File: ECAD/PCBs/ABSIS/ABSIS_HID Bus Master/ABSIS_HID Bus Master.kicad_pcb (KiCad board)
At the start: 2 copper layers, 90.8 x 53.3 mm, 19 parts, among them J1 Molex_Mini-Fit_Jr._2x04, J2 Mini-Fit Jr. 2x03, U0 ProMicro_5V/16Hz, U1 MAX487EESA+T

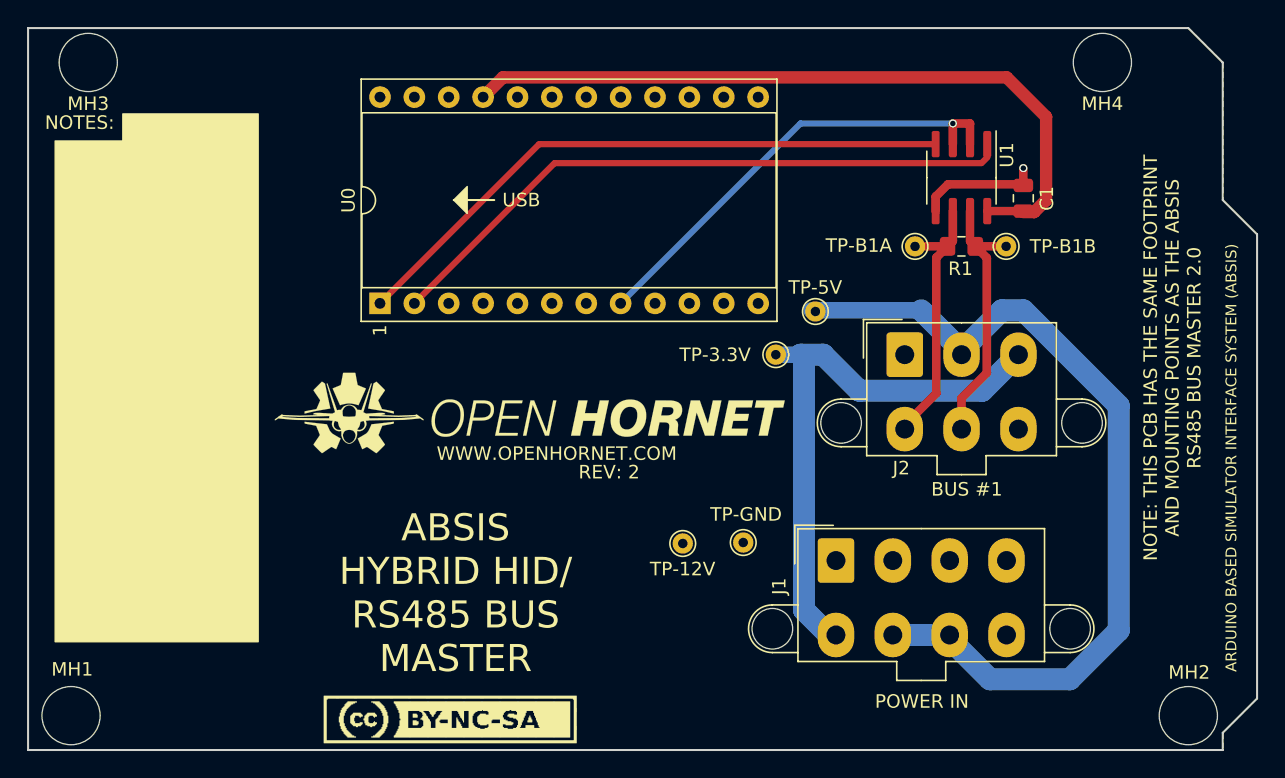
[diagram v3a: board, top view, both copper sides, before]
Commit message: Updated ABSIS_HID Bus Master
Added 1N5819WS (D1) between 12V Supply and RAW pin of Pro-Micro
Updated to Rev 3.
Closes #995
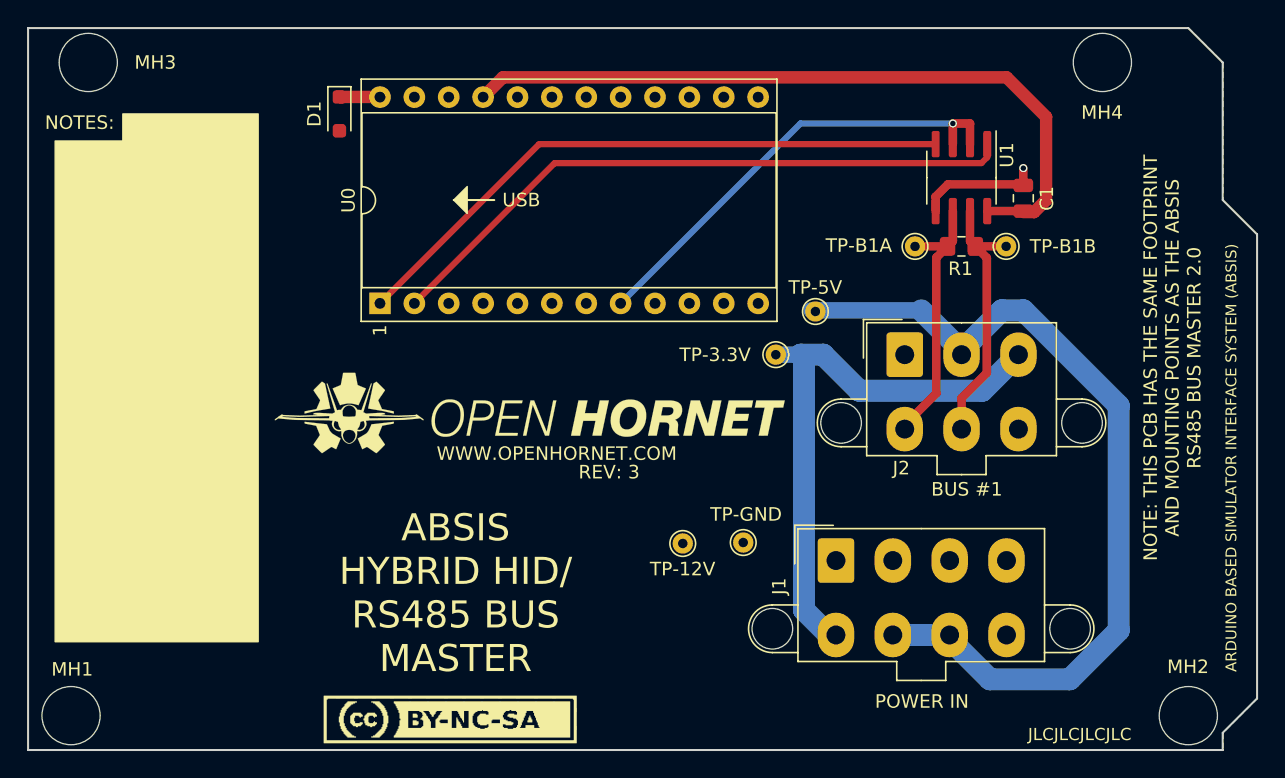
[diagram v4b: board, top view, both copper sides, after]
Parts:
- added D1: 1N5819WS, Diode_SMD:D_SOD-323_HandSoldering, F.Cu at (137.2, 74.7)
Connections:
- U0 pad 24: /+12V_SUPPLY -> Net-(D1-K)
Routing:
- net Net-(D1-K): track 0.00 -> 3.00 mm
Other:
- board text added: "JLCJLCJLCJLC"
- board text added: "REV: 3"
- board text removed: "REV: 2"
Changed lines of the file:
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@@
   (title_block
     (title "ABSIS HID Bus Master")
-    (date "2023-02-10")
-    (rev "2")
+    (date "2023-11-05")
+    (rev "3")
     (company "www.openhornet.com")
     (comment 1 "License:  CC BY-NC-SA")
@@
   (net 25 "unconnected-(U0-A3-Pad20)")
   (net 26 "/TX0_D1")
+  (net 27 "Net-(D1-K)")
   (footprint "OH_Footprints:MountingHole_6-32_PHS" (layer "F.Cu")
     (at 117.348 119.126)
@@
     (property "ki_description" "6-32 PHS Hole with back fill keepout area, 4.3mm")
     (attr through_hole board_only exclude_from_pos_files exclude_from_bom)
-    (fp_text reference "MH2" (at 0.065 -3.19) (layer "F.SilkS")
+    (fp_text reference "MH2" (at -0.025 -3.61) (layer "F.SilkS")
         (effects (font (size 1 1) (thickness 0.15)))
     )
@@
     (property "ki_description" "6-32 PHS Hole with back fill keepout area, 4.3mm")
     (attr through_hole board_only exclude_from_pos_files exclude_from_bom)
-    (fp_text reference "MH3" (at 0 3.048) (layer "F.SilkS")
+    (fp_text reference "MH3" (at 4.955 0) (layer "F.SilkS")
         (effects (font (size 1 1) (thickness 0.15)))
     )
@@
     (property "ki_description" "6-32 PHS Hole with back fill keepout area, 4.3mm")
     (attr through_hole board_only exclude_from_pos_files exclude_from_bom)
-    (fp_text reference "MH4" (at 0 3.048) (layer "F.SilkS")
+    (fp_text reference "MH4" (at -0.025 3.7) (layer "F.SilkS")
         (effects (font (size 1 1) (thickness 0.15)))
     )
@@
     (property "Sheetname" "")
     (property "Silkscreen" "POWER IN")
-    (attr through_hole)
+    (attr through_hole exclude_from_pos_files)
     (fp_text reference "J1" (at -4.191 1.905 90) (layer "F.SilkS")
         (effects (font (size 1 1) (thickness 0.15)))
@@
     (property "ki_description" "Generic connector, double row, 02x03, top/bottom pin numbering scheme (row 1: 1...pins_per_row, row2: pins_per_row+1 ... num_pins), script generated (kicad-library-utils/schlib/autogen/connector/)")
     (property "ki_keywords" "connector")
-    (attr through_hole)
+    (attr through_hole exclude_from_pos_files)
     (fp_text reference "J2" (at -0.254 8.382) (layer "F.SilkS")
         (effects (font (size 1 1) (thickness 0.15)))
@@
     (property "Sheetname" "")
     (property "ki_description" "CC License, BY-NC-SA, no symbols, Small")
-    (attr board_only exclude_from_bom)
+    (attr board_only exclude_from_pos_files exclude_from_bom)
     (fp_text reference "LOGO3" (at 0 5) (layer "F.SilkS") hide
         (effects (font (size 1.524 1.524) (thickness 0.3)))
@@
     (property "Sheetfile" "ABSIS_HID Bus Master.kicad_sch")
     (property "Sheetname" "")
-    (attr through_hole)
+    (attr through_hole exclude_from_pos_files)
     (fp_text reference "U0" (at 7.62 -2.33 90) (layer "F.SilkS")
         (effects (font (size 1 1) (thickness 0.15)))
@@
       (net 1 "GND") (pinfunction "GND") (pintype "power_in"))
     (pad "24" thru_hole oval (at 15.24 0 90) (size 1.6 1.6) (drill 0.8) (layers "*.Cu" "*.Mask")
-      (net 3 "/+12V_SUPPLY") (pinfunction "RAW") (pintype "power_in"))
+      (net 27 "Net-(D1-K)") (pinfunction "RAW") (pintype "power_in"))
     (model "${KICAD_USER_OH_3DMODELS}/DIP-24_W15.24mm_Socket.step"
       (offset (xyz 0 0 0))
@@
       (net 4 "/+5V_SUPPLY") (pinfunction "1") (pintype "passive"))
   )
+  (footprint "Diode_SMD:D_SOD-323_HandSoldering" (layer "F.Cu")
+    (at 137.173 74.666 -90)
+    (descr "SOD-323")
+    (tags "SOD-323")
+    (property "LCSC" "C191023")
+    (property "Manufacturer PN" "1N5819WS")
+    (property "Sheetfile" "ABSIS_HID Bus Master.kicad_sch")
+    (property "Sheetname" "")
+    (property "ki_description" "Schottky diode")
+    (property "ki_keywords" "diode Schottky")
+    (attr smd)
+    (fp_text reference "D1" (at 0 1.85 90) (layer "F.SilkS")
+        (effects (font (size 1 1) (thickness 0.15)))
+    )
+    (fp_text value "1N5819WS" (at 0.1 1.9 90) (layer "F.Fab")
+        (effects (font (size 1 1) (thickness 0.15)))
+    )
+    (fp_text user "${REFERENCE}" (at 0 -1.85 90) (layer "F.Fab")
+        (effects (font (size 1 1) (thickness 0.15)))
+    )
+    (fp_line (start -2.01 -0.85) (end -2.01 0.85)
+      (stroke (width 0.12) (type solid)) (layer "F.SilkS"))
+    (fp_line (start -2.01 -0.85) (end 1.25 -0.85)
+      (stroke (width 0.12) (type solid)) (layer "F.SilkS"))
+    (fp_line (start -2.01 0.85) (end 1.25 0.85)
+      (stroke (width 0.12) (type solid)) (layer "F.SilkS"))
+    (fp_line (start -2 -0.95) (end -2 0.95)
+      (stroke (width 0.05) (type solid)) (layer "F.CrtYd"))
+    (fp_line (start -2 -0.95) (end 2 -0.95)
+      (stroke (width 0.05) (type solid)) (layer "F.CrtYd"))
+    (fp_line (start -2 0.95) (end 2 0.95)
+      (stroke (width 0.05) (type solid)) (layer "F.CrtYd"))
+    (fp_line (start 2 -0.95) (end 2 0.95)
+      (stroke (width 0.05) (type solid)) (layer "F.CrtYd"))
+    (fp_line (start -0.9 -0.7) (end 0.9 -0.7)
+      (stroke (width 0.1) (type solid)) (layer "F.Fab"))
+    (fp_line (start -0.9 0.7) (end -0.9 -0.7)
+      (stroke (width 0.1) (type solid)) (layer "F.Fab"))
+    (fp_line (start -0.3 -0.35) (end -0.3 0.35)
+      (stroke (width 0.1) (type solid)) (layer "F.Fab"))
+    (fp_line (start -0.3 0) (end -0.5 0)
+      (stroke (width 0.1) (type solid)) (layer "F.Fab"))
+    (fp_line (start -0.3 0) (end 0.2 -0.35)
+      (stroke (width 0.1) (type solid)) (layer "F.Fab"))
+    (fp_line (start 0.2 -0.35) (end 0.2 0.35)
+      (stroke (width 0.1) (type solid)) (layer "F.Fab"))
+    (fp_line (start 0.2 0) (end 0.45 0)
+      (stroke (width 0.1) (type solid)) (layer "F.Fab"))
+    (fp_line (start 0.2 0.35) (end -0.3 0)
+      (stroke (width 0.1) (type solid)) (layer "F.Fab"))
+    (fp_line (start 0.9 -0.7) (end 0.9 0.7)
+      (stroke (width 0.1) (type solid)) (layer "F.Fab"))
+    (fp_line (start 0.9 0.7) (end -0.9 0.7)
+      (stroke (width 0.1) (type solid)) (layer "F.Fab"))
+    (pad "1" smd roundrect (at -1.25 0 270) (size 1 1) (layers "F.Cu" "F.Paste" "F.Mask") (roundrect_rratio 0.25)
+      (net 27 "Net-(D1-K)") (pinfunction "K") (pintype "passive"))
+    (pad "2" smd roundrect (at 1.25 0 270) (size 1 1) (layers "F.Cu" "F.Paste" "F.Mask") (roundrect_rratio 0.25)
+      (net 3 "/+12V_SUPPLY") (pinfunction "A") (pintype "passive"))
+    (model "${KICAD6_3DMODEL_DIR}/Diode_SMD.3dshapes/D_SOD-323.wrl"
+      (offset (xyz 0 0 0))
+      (scale (xyz 1 1 1))
+      (rotate (xyz 0 0 0))
+    )
+  )
   (footprint "OH_Footprints:TestPoint_THTPad_D1.5mm_Drill0.7mm" (layer "F.Cu")
     (at 169.418 92.456)
@@
     (effects (font (size 1 1) (thickness 0.15)))
   )
-  (gr_text "REV: 2" (at 157.103 101.136) (layer "F.SilkS")
+  (gr_text "REV: 3" (at 157.103 101.136) (layer "F.SilkS")
     (effects (font (size 1 1) (thickness 0.15)))
   )
@@
     (effects (font (size 0.8 0.8) (thickness 0.15)))
   )
+  (gr_text "JLCJLCJLCJLC" (at 191.873 120.516) (layer "F.SilkS")
+    (effects (font (size 0.9 0.9) (thickness 0.15)))
+  )
   (gr_text "NOTES:" (at 117.983 75.311) (layer "F.SilkS")
     (effects (font (size 1 1) (thickness 0.2)))
@@
   (segment (start 151.939 76.9) (end 140.173 88.666) (width 0.4572) (layer "F.Cu") (net 26))
   (segment (start 181.229 76.9) (end 151.939 76.9) (width 0.4572) (layer "F.Cu") (net 26))
+  (segment (start 137.173 73.416) (end 140.163 73.416) (width 0.9144) (layer "F.Cu") (net 27))
+  (segment (start 140.163 73.416) (end 140.173 73.426) (width 0.9144) (layer "F.Cu") (net 27))
   (zone (net 3) (net_name "/+12V_SUPPLY") (layer "F.Cu") (hatch edge 0.508)
     (connect_pads (clearance 0.508))

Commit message: Updated mounting holes
Updated PCB mounting holes to M3 clearance holes.
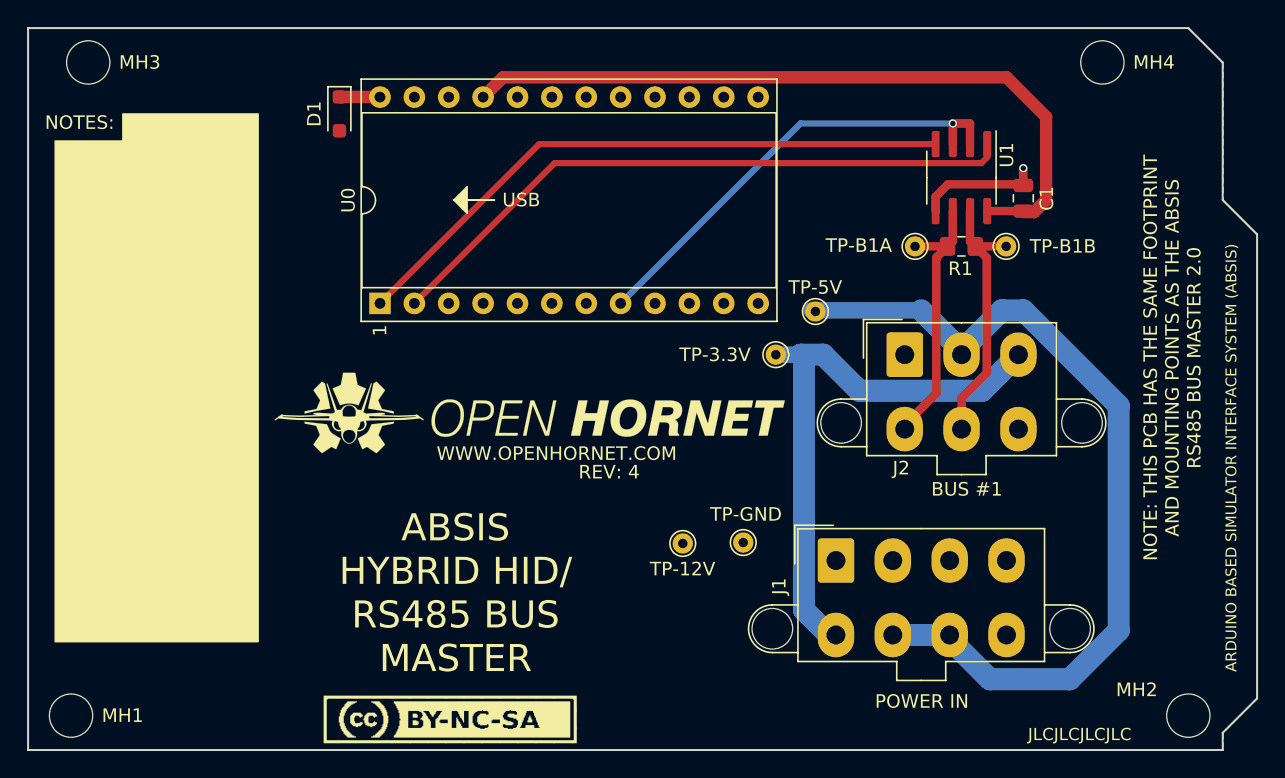
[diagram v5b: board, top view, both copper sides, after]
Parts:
- MH1, MH2, MH3, MH4: footprint OH_Footprints:MountingHole_6-32_PHS -> OH_Footprints:MountingHole_3.2mm_M3_DIN965
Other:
- board text added: "REV: 4"
- board text removed: "REV: 3"
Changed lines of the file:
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@@
   (title_block
     (title "ABSIS HID Bus Master")
-    (date "2023-11-05")
-    (rev "3")
+    (date "2023-12-10")
+    (rev "4")
     (company "www.openhornet.com")
     (comment 1 "License:  CC BY-NC-SA")
@@
   (net 26 "/TX0_D1")
   (net 27 "Net-(D1-K)")
-  (footprint "OH_Footprints:MountingHole_6-32_PHS" (layer "F.Cu")
+  (footprint "OH_Footprints:MountingHole_3.2mm_M3_DIN965" (layer "F.Cu")
     (at 117.348 119.126)
-    (descr "Mounting Hole for 6x32 PHS, 4.3mm")
+    (descr "Mounting Hole 3.2mm, no annular, M3, DIN965")
+    (tags "mounting hole 3.2mm no annular m3 din965")
     (property "Sheetfile" "ABSIS_HID Bus Master.kicad_sch")
     (property "Sheetname" "")
+    (property "Sim.Enable" "0")
     (property "exclude_from_bom" "")
-    (property "ki_description" "6-32 PHS Hole with back fill keepout area, 4.3mm")
-    (attr through_hole board_only exclude_from_pos_files exclude_from_bom)
-    (fp_text reference "MH1" (at 0.085 -3.42) (layer "F.SilkS")
+    (property "ki_description" "M3 hole with back fill keepout area, 3.2mm, DIN965")
+    (attr exclude_from_pos_files exclude_from_bom)
+    (fp_text reference "MH1" (at 3.81 0) (layer "F.SilkS")
         (effects (font (size 1 1) (thickness 0.15)))
     )
-    (fp_text value "6x32 / 4mm" (at -0.025 0) (layer "F.Fab") hide
+    (fp_text value "6x32 / 4mm" (at 0 8.636) (layer "F.Fab") hide
         (effects (font (size 1 1) (thickness 0.15)))
     )
-    (pad "" np_thru_hole circle (at 0 0) (size 4.3 4.3) (drill 4.3) (layers "F&B.Cu" "*.Mask")
-      (clearance 0.54))
+    (pad "" np_thru_hole circle (at 0 0) (size 3.2 3.2) (drill 3.2) (layers "F&B.Cu" "*.Mask")
+      (clearance 0.5))
   )
-  (footprint "OH_Footprints:MountingHole_6-32_PHS" (layer "F.Cu")
+  (footprint "OH_Footprints:MountingHole_3.2mm_M3_DIN965" (layer "F.Cu")
     (at 199.898 119.126)
-    (descr "Mounting Hole for 6x32 PHS, 4.3mm")
+    (descr "Mounting Hole 3.2mm, no annular, M3, DIN965")
+    (tags "mounting hole 3.2mm no annular m3 din965")
     (property "Sheetfile" "ABSIS_HID Bus Master.kicad_sch")
     (property "Sheetname" "")
+    (property "Sim.Enable" "0")
     (property "exclude_from_bom" "")
-    (property "ki_description" "6-32 PHS Hole with back fill keepout area, 4.3mm")
-    (attr through_hole board_only exclude_from_pos_files exclude_from_bom)
-    (fp_text reference "MH2" (at -0.025 -3.61) (layer "F.SilkS")
+    (property "ki_description" "M3 hole with back fill keepout area, 3.2mm, DIN965")
+    (attr exclude_from_pos_files exclude_from_bom)
+    (fp_text reference "MH2" (at -3.81 -1.905) (layer "F.SilkS")
         (effects (font (size 1 1) (thickness 0.15)))
     )
-    (fp_text value "6x32 / 4mm" (at -0.025 0) (layer "F.Fab") hide
+    (fp_text value "6x32 / 4mm" (at 0 8.636) (layer "F.Fab") hide
         (effects (font (size 1 1) (thickness 0.15)))
     )
-    (pad "" np_thru_hole circle (at 0 0) (size 4.3 4.3) (drill 4.3) (layers "F&B.Cu" "*.Mask")
-      (clearance 0.54))
+    (pad "" np_thru_hole circle (at 0 0) (size 3.2 3.2) (drill 3.2) (layers "F&B.Cu" "*.Mask")
+      (clearance 0.5))
   )
-  (footprint "OH_Footprints:MountingHole_6-32_PHS" (layer "F.Cu")
+  (footprint "OH_Footprints:MountingHole_3.2mm_M3_DIN965" (layer "F.Cu")
     (at 118.618 70.866)
-    (descr "Mounting Hole for 6x32 PHS, 4.3mm")
+    (descr "Mounting Hole 3.2mm, no annular, M3, DIN965")
+    (tags "mounting hole 3.2mm no annular m3 din965")
     (property "Sheetfile" "ABSIS_HID Bus Master.kicad_sch")
     (property "Sheetname" "")
+    (property "Sim.Enable" "0")
     (property "exclude_from_bom" "")
-    (property "ki_description" "6-32 PHS Hole with back fill keepout area, 4.3mm")
-    (attr through_hole board_only exclude_from_pos_files exclude_from_bom)
-    (fp_text reference "MH3" (at 4.955 0) (layer "F.SilkS")
+    (property "ki_description" "M3 hole with back fill keepout area, 3.2mm, DIN965")
+    (attr exclude_from_pos_files exclude_from_bom)
+    (fp_text reference "MH3" (at 3.81 0) (layer "F.SilkS")
         (effects (font (size 1 1) (thickness 0.15)))
     )
-    (fp_text value "6x32 / 4mm" (at -0.025 0) (layer "F.Fab") hide
+    (fp_text value "6x32 / 4mm" (at 0 8.636) (layer "F.Fab") hide
         (effects (font (size 1 1) (thickness 0.15)))
     )
-    (pad "" np_thru_hole circle (at 0 0) (size 4.3 4.3) (drill 4.3) (layers "F&B.Cu" "*.Mask")
-      (clearance 0.54))
+    (pad "" np_thru_hole circle (at 0 0) (size 3.2 3.2) (drill 3.2) (layers "F&B.Cu" "*.Mask")
+      (clearance 0.5))
   )
-  (footprint "OH_Footprints:MountingHole_6-32_PHS" (layer "F.Cu")
+  (footprint "OH_Footprints:MountingHole_3.2mm_M3_DIN965" (layer "F.Cu")
     (at 193.548 70.866)
-    (descr "Mounting Hole for 6x32 PHS, 4.3mm")
+    (descr "Mounting Hole 3.2mm, no annular, M3, DIN965")
+    (tags "mounting hole 3.2mm no annular m3 din965")
     (property "Sheetfile" "ABSIS_HID Bus Master.kicad_sch")
     (property "Sheetname" "")
+    (property "Sim.Enable" "0")
     (property "exclude_from_bom" "")
-    (property "ki_description" "6-32 PHS Hole with back fill keepout area, 4.3mm")
-    (attr through_hole board_only exclude_from_pos_files exclude_from_bom)
-    (fp_text reference "MH4" (at -0.025 3.7) (layer "F.SilkS")
+    (property "ki_description" "M3 hole with back fill keepout area, 3.2mm, DIN965")
+    (attr exclude_from_pos_files exclude_from_bom)
+    (fp_text reference "MH4" (at 3.81 0) (layer "F.SilkS")
         (effects (font (size 1 1) (thickness 0.15)))
     )
-    (fp_text value "6x32 / 4mm" (at -0.025 0) (layer "F.Fab") hide
+    (fp_text value "6x32 / 4mm" (at 0 8.636) (layer "F.Fab") hide
         (effects (font (size 1 1) (thickness 0.15)))
     )
-    (pad "" np_thru_hole circle (at 0 0) (size 4.3 4.3) (drill 4.3) (layers "F&B.Cu" "*.Mask")
-      (clearance 0.54))
+    (pad "" np_thru_hole circle (at 0 0) (size 3.2 3.2) (drill 3.2) (layers "F&B.Cu" "*.Mask")
+      (clearance 0.5))
   )
   (footprint "OH_Footprints:TestPoint_THTPad_D1.5mm_Drill0.7mm" (layer "F.Cu")
@@
     (effects (font (size 1 1) (thickness 0.15)))
   )
-  (gr_text "REV: 3" (at 157.103 101.136) (layer "F.SilkS")
+  (gr_text "REV: 4" (at 157.103 101.136) (layer "F.SilkS")
     (effects (font (size 1 1) (thickness 0.15)))
   )
